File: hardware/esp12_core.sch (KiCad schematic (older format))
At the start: 6 parts

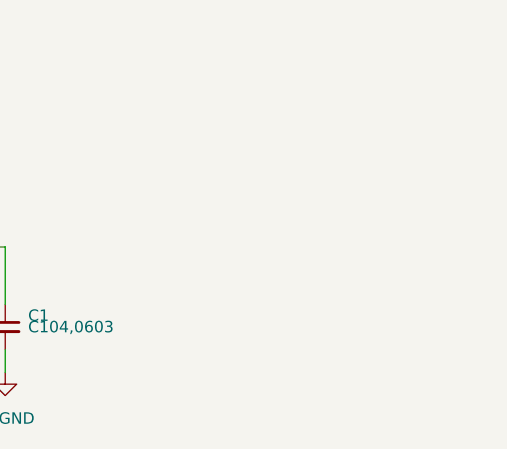
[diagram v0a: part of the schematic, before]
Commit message: update esp12 core,
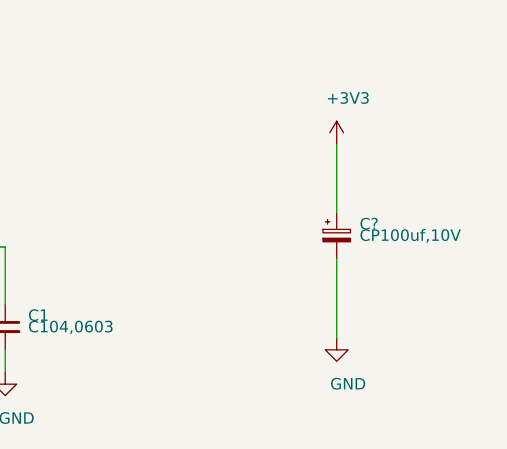
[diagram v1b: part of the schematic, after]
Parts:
- added C?: CP100uf,10V, Capacitor_SMD:CP_Elec_6.3x5.3, symbol taobao-cp:CP100uf,10V
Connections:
- net +3V3: now also C?.1
- net GND: now also C?.2
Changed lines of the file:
@@
 	2550 2400 2550 2200
 Connection ~ 2550 2200
+$Comp
+L power:+3V3 #PWR?
+U 1 1 5CD53342
+P 5600 1950
+F 0 "#PWR?" H 5600 1800 50  0001 C CNN
+F 1 "+3V3" H 5650 2150 50  0000 C CNN
+F 2 "" H 5600 1950 50  0001 C CNN
+F 3 "" H 5600 1950 50  0001 C CNN
+	1    5600 1950
+	1    0    0    -1
+$EndComp
+$Comp
+L taobao-cp:CP100uf,10V C?
+U 1 1 5CD53834
+P 5600 2350
+F 0 "C?" H 5700 2400 50  0000 L CNN
+F 1 "CP100uf,10V" H 5700 2350 50  0000 L CNN
+F 2 "Capacitor_SMD:CP_Elec_6.3x5.3" H 5600 2350 50  0001 C CNN
+F 3 "~" H 5600 2350 50  0001 C CNN
+	1    5600 2350
+	1    0    0    -1
+$EndComp
+$Comp
+L power:GND #PWR?
+U 1 1 5CD53C45
+P 5600 2800
+F 0 "#PWR?" H 5600 2550 50  0001 C CNN
+F 1 "GND" H 5650 2600 50  0000 C CNN
+F 2 "" H 5600 2800 50  0001 C CNN
+F 3 "" H 5600 2800 50  0001 C CNN
+	1    5600 2800
+	1    0    0    -1
+$EndComp
+Wire Wire Line
+	5600 1950 5600 2250
+Wire Wire Line
+	5600 2450 5600 2800
 $EndSCHEMATC

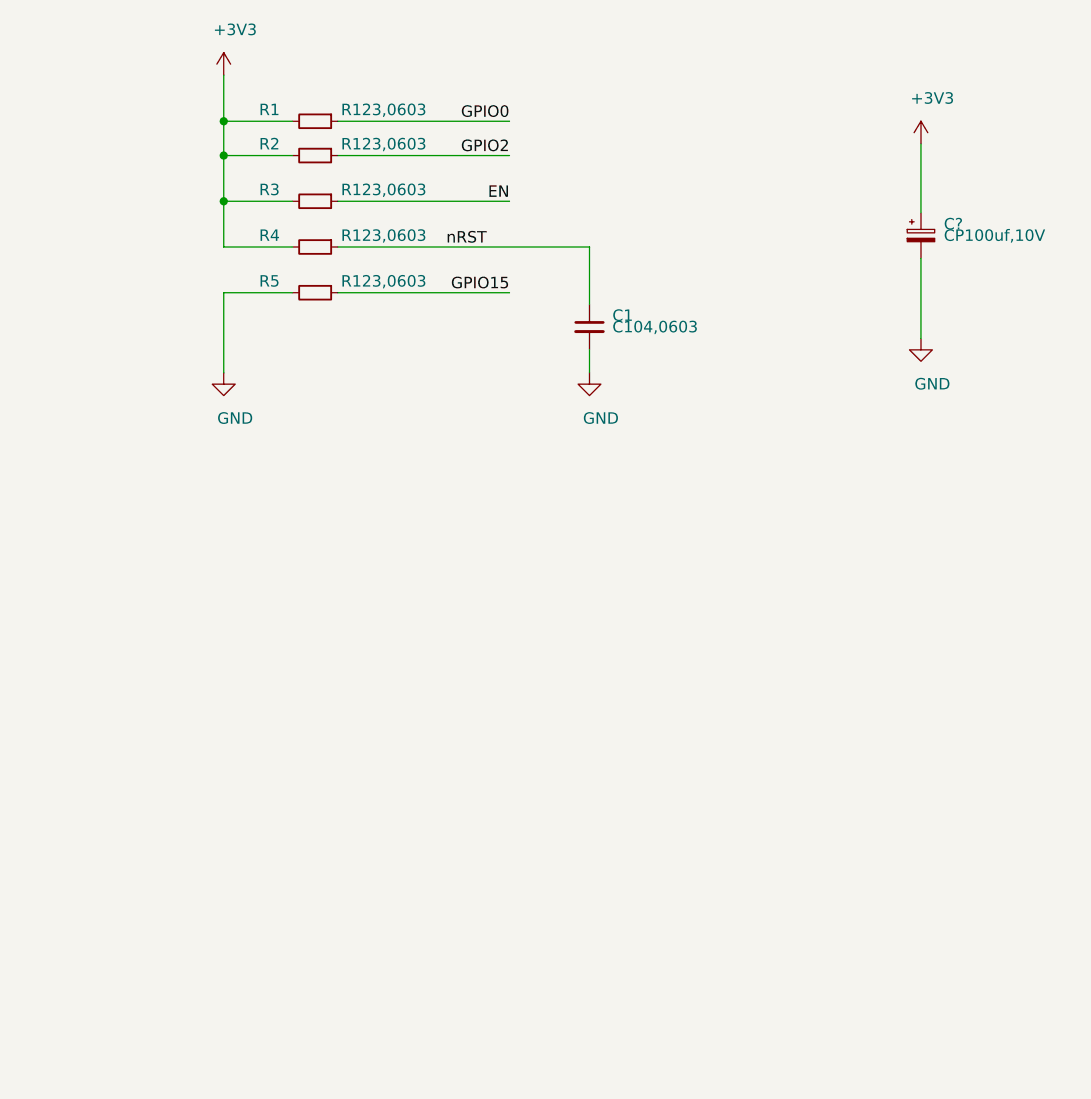
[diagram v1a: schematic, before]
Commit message: update esp12 core,
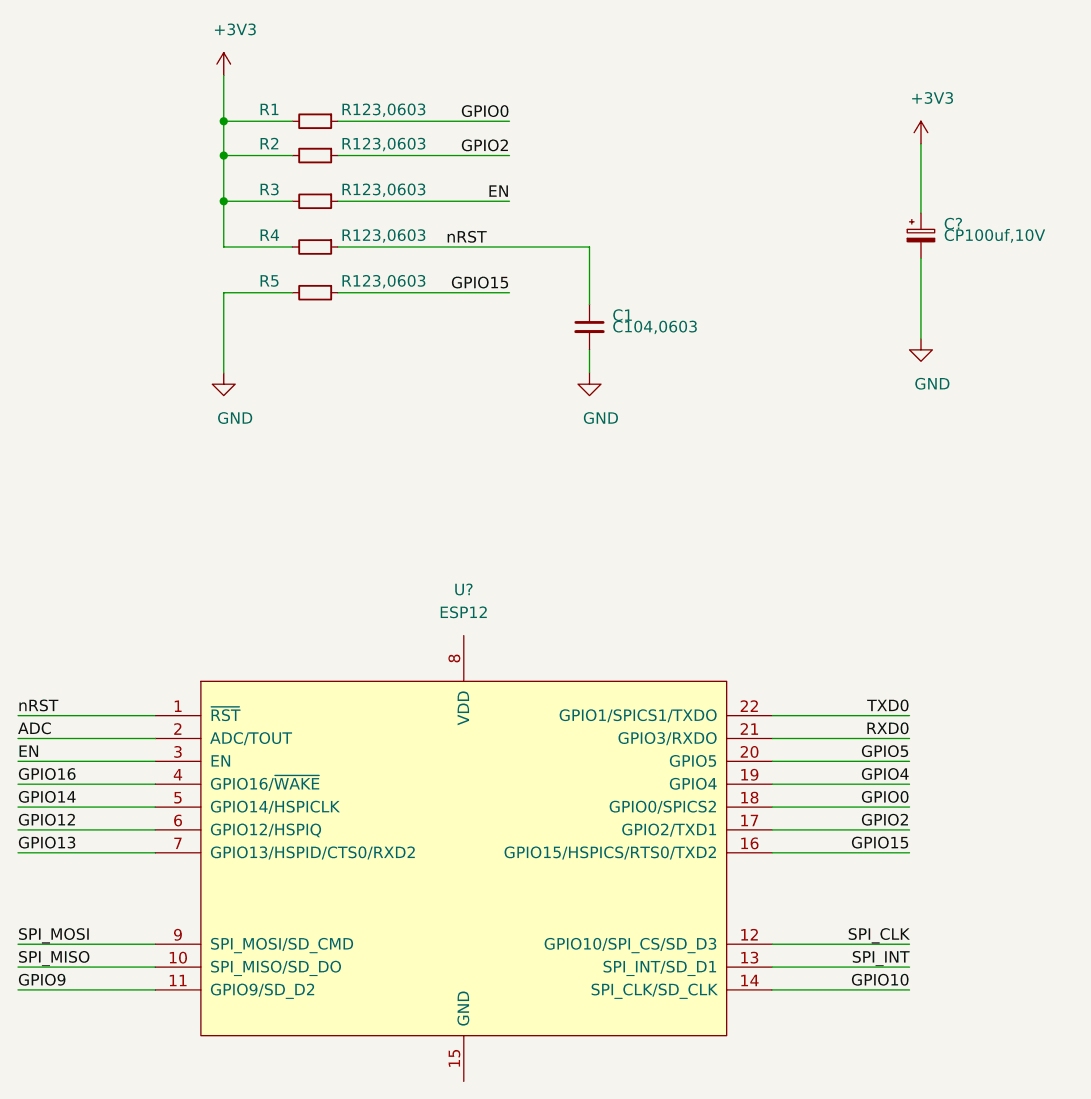
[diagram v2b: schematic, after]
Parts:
- added U?: ESP12, footprint-lib:ESP-12, symbol taobao-components:ESP12
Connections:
- net EN: now also U?.3 (EN)
- net GPIO0: now also U?.18 (GPIO0/SPICS2)
- net GPIO15: now also U?.16 (GPIO15/HSPICS/RTS0/TXD2)
- net GPIO2: now also U?.17 (GPIO2/TXD1)
- net nRST: now also U?.1 (~RST~)
- new net ADC: U?.2 (ADC/TOUT)
- new net GPIO10: U?.14 (SPI_CLK/SD_CLK)
- new net GPIO12: U?.6 (GPIO12/HSPIQ)
- new net GPIO13: U?.7 (GPIO13/HSPID/CTS0/RXD2)
- new net GPIO14: U?.5 (GPIO14/HSPICLK)
- new net GPIO16: U?.4 (GPIO16/~WAKE~)
- new net GPIO4: U?.19 (GPIO4)
- new net GPIO5: U?.20 (GPIO5)
- new net GPIO9: U?.11 (GPIO9/SD_D2)
- new net RXD0: U?.21 (GPIO3/RXDO)
- new net SPI_CLK: U?.12 (GPIO10/SPI_CS/SD_D3)
- new net SPI_INT: U?.13 (SPI_INT/SD_D1)
- new net SPI_MISO: U?.10 (SPI_MISO/SD_DO)
- new net SPI_MOSI: U?.9 (SPI_MOSI/SD_CMD)
- new net TXD0: U?.22 (GPIO1/SPICS1/TXDO)
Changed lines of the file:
@@
 Wire Wire Line
 	5600 2450 5600 2800
+Text Label 1650 4450 0    50   ~ 0
+nRST
+Text Label 1650 4550 0    50   ~ 0
+ADC
+Text Label 1650 4650 0    50   ~ 0
+EN
+Text Label 1650 4750 0    50   ~ 0
+GPIO16
+Text Label 1650 4850 0    50   ~ 0
+GPIO14
+Text Label 1650 4950 0    50   ~ 0
+GPIO12
+Text Label 1650 5050 0    50   ~ 0
+GPIO13
+Text Label 1650 5450 0    50   ~ 0
+SPI_MOSI
+Text Label 1650 5550 0    50   ~ 0
+SPI_MISO
+Text Label 1650 5650 0    50   ~ 0
+GPIO9
+Wire Wire Line
+	1650 4450 2250 4450
+Wire Wire Line
+	1650 4550 2250 4550
+Wire Wire Line
+	1650 4650 2250 4650
+Wire Wire Line
+	1650 4750 2250 4750
+Wire Wire Line
+	1650 4850 2250 4850
+Wire Wire Line
+	1650 4950 2250 4950
+Wire Wire Line
+	1650 5050 2250 5050
+Wire Wire Line
+	1650 5450 2250 5450
+Wire Wire Line
+	1650 5550 2250 5550
+Wire Wire Line
+	1650 5650 2250 5650
+$Comp
+L taobao-components:ESP12 U?
+U 1 1 5CD4D9E6
+P 3600 5200
+F 0 "U?" H 3600 6500 50  0000 C CNN
+F 1 "ESP12" H 3600 6400 50  0000 C CNN
+F 2 "footprint-lib:ESP-12" H 3650 4500 50  0001 C CNN
+F 3 "" H 3650 4500 50  0001 C CNN
+	1    3600 5200
+	1    0    0    -1
+$EndComp
+Text Label 5550 4450 2    50   ~ 0
+TXD0
+Text Label 5550 4550 2    50   ~ 0
+RXD0
+Text Label 5550 4650 2    50   ~ 0
+GPIO5
+Text Label 5550 4750 2    50   ~ 0
+GPIO4
+Text Label 5550 4850 2    50   ~ 0
+GPIO0
+Text Label 5550 4950 2    50   ~ 0
+GPIO2
+Text Label 5550 5050 2    50   ~ 0
+GPIO15
+Text Label 5550 5450 2    50   ~ 0
+SPI_CLK
+Text Label 5550 5550 2    50   ~ 0
+SPI_INT
+Text Label 5550 5650 2    50   ~ 0
+GPIO10
+Wire Wire Line
+	5550 4450 4950 4450
+Wire Wire Line
+	5550 4550 4950 4550
+Wire Wire Line
+	5550 4650 4950 4650
+Wire Wire Line
+	5550 4750 4950 4750
+Wire Wire Line
+	5550 4850 4950 4850
+Wire Wire Line
+	5550 4950 4950 4950
+Wire Wire Line
+	5550 5050 4950 5050
+Wire Wire Line
+	5550 5450 4950 5450
+Wire Wire Line
+	5550 5550 4950 5550
+Wire Wire Line
+	5550 5650 4950 5650
 $EndSCHEMATC
